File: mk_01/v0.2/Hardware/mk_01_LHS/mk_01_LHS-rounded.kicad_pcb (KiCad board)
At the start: 2 copper layers, 165.1 x 102.9 mm, 79 parts, among them SW1 SW_Push_Dual, U1 nice_nano

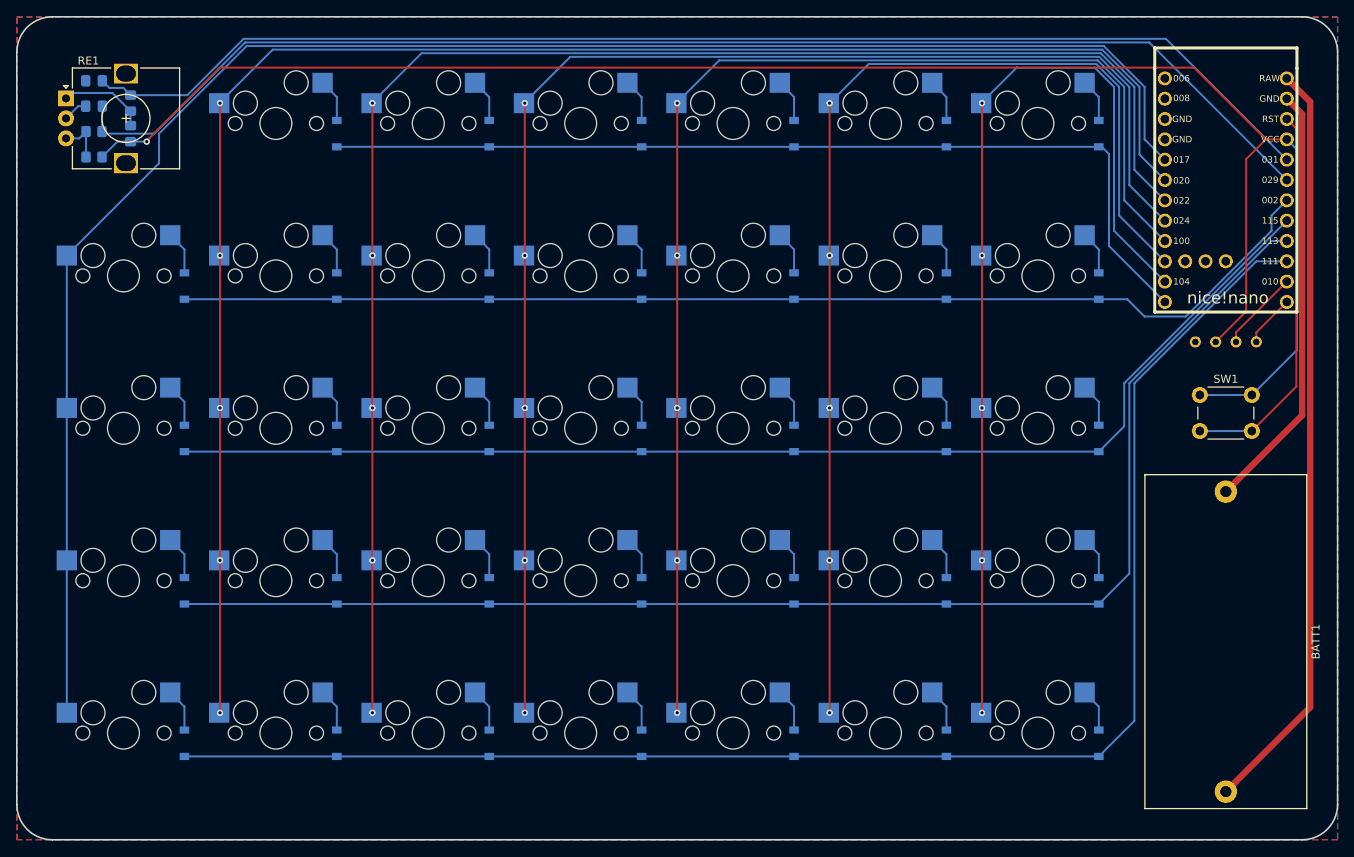
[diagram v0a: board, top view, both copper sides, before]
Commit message: PCB completed and rounded
The PCB is pretty much complete for the left hand side, and I've generated a seperate file with rounded tracks using the round tracks plugin.
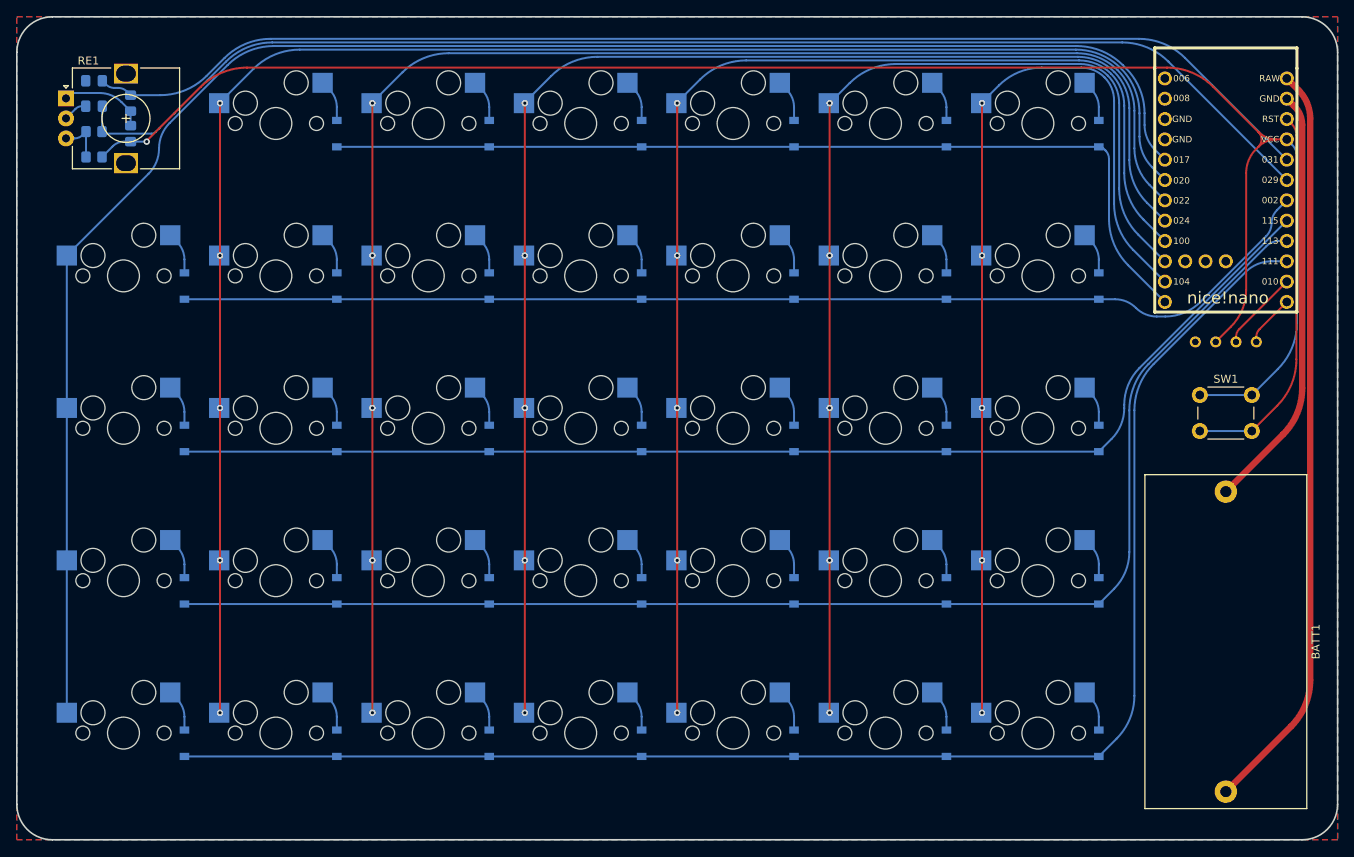
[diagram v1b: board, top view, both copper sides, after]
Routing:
- net col0: track 217.2 -> 215.4 mm
- net col1: track 208.9 -> 207.5 mm
- net col2: track 191.6 -> 190.2 mm
- net col3: track 174.4 -> 173.0 mm
- net col4: track 157.1 -> 155.8 mm
- net Net-(C7-Pad2): track 158.0 -> 156.7 mm
- net col5: track 139.8 -> 138.5 mm
- net col6: track 122.6 -> 121.5 mm
- net VCC: track 225.7 -> 226.9 mm
- net row4: track 188.2 -> 187.2 mm
- net row1: track 145.8 -> 144.9 mm
- net row2: track 153.5 -> 152.6 mm
- net Net-(C8-Pad1): track 163.2 -> 162.4 mm
- net row3: track 170.5 -> 169.7 mm
- net Net-(U1-Pad24): track 94.7 -> 94.1 mm
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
